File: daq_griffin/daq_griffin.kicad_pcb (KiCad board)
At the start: 4 copper layers, 85 x 120 mm, 191 parts, among them J13 SENSOR, J14 SENSOR, J15 SENSOR, J16 SENSOR, J17 SENSOR, J18 SENSOR, J19 SENSOR, J20 SENSOR, J21 SENSOR, J22 SENSOR, J23 SENSOR, J24 SENSOR, J25 POWER_12V, J26 I2C Header, J27 CAN Header, U13 ADS8866, U14 ADS8866, U15 ADS8866, U16 ADS8866, U17 ADS8866, U18 ADS8866, U19 ADS8866, U20 ADS8866, U21 ADS8866, U22 ADS8866, U23 ADS8866, U24 ADS8866, U25 TPS54302, U26 Teensy4.1, U29 REF6050xDGK, U30 TLV70933, U55 TCAN3414

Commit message: Add files via upload
one 5 V plane contained only 2 connections, so it was replaced with a single wire
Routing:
- net +5V: track 108.8 -> 127.1 mm, vias 4 -> 2
- removed copper zone on In1.Cu, net +5V
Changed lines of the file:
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@@
 	)
 	(via
-		(at 154.4 80.4)
-		(size 0.8)
-		(drill 0.4)
-		(layers "F.Cu" "B.Cu")
-		(net 7)
-	)
-	(via
 		(at 138.888 73.438)
 		(size 0.8)
@@
 	)
 	(via
-		(at 118.4 79.2)
-		(size 0.8)
-		(drill 0.4)
-		(layers "F.Cu" "B.Cu")
-		(net 7)
-	)
-	(via
 		(at 125.1985 73.438)
 		(size 0.8)
@@
 	)
 	(segment
+		(start 138.888 73.438)
+		(end 147.438 73.438)
+		(width 1)
+		(layer "B.Cu")
+		(net 7)
+	)
+	(segment
 		(start 154.42 89.408)
 		(end 154.42 80.42)
@@
 	)
 	(segment
-		(start 154.42 80.42)
-		(end 154.4 80.4)
-		(width 1)
-		(layer "B.Cu")
-		(net 7)
-	)
-	(segment
 		(start 123.971001 83.759)
 		(end 123.971001 81.99)
@@
 	)
 	(segment
-		(start 118.304501 79.104501)
-		(end 118.4 79.2)
-		(width 1)
-		(layer "B.Cu")
-		(net 7)
-	)
-	(segment
 		(start 122.495501 75.438)
 		(end 123.1985 75.438)
@@
 	)
 	(segment
+		(start 147.438 73.438)
+		(end 154.42 80.42)
+		(width 1)
+		(layer "B.Cu")
+		(net 7)
+	)
+	(segment
 		(start 166.584 91.273)
 		(end 166.584 93.853)
@@
 			)
 		)
-	)
-	(zone
-		(net 7)
-		(net_name "+5V")
-		(layer "In1.Cu")
-		(hatch edge 0.508)
-		(connect_pads
-			(clearance 0)
-		)
-		(min_thickness 0.254)
-		(filled_areas_thickness no)
-		(fill yes
-			(thermal_gap 0.508)
-			(thermal_bridge_width 0.508)
-		)
-		(polygon
-			(pts
-				(xy 169.2 81.6) (xy 110.6 81.6) (xy 110.6 77.1) (xy 169.2 77.1)
-			)
-		)

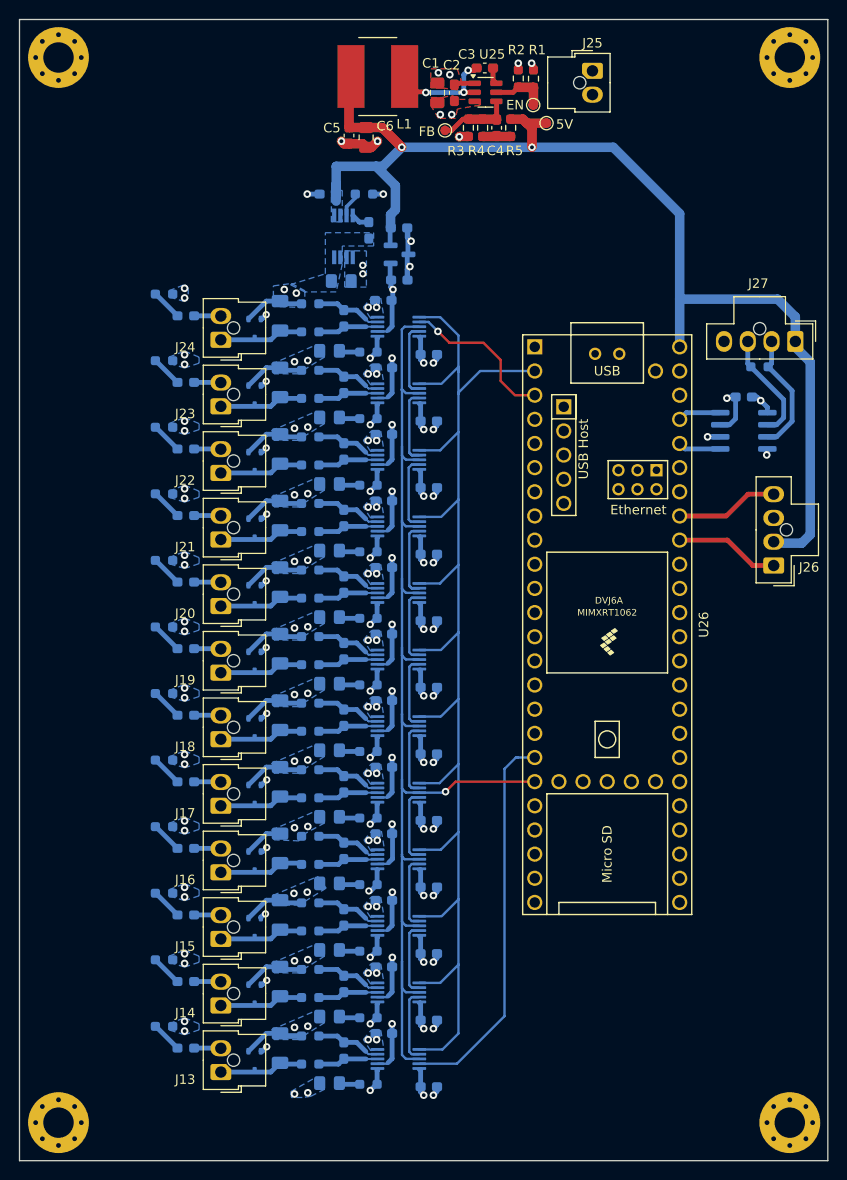
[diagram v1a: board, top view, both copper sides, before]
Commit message: Add thermocouple connectors and minor layout changes.
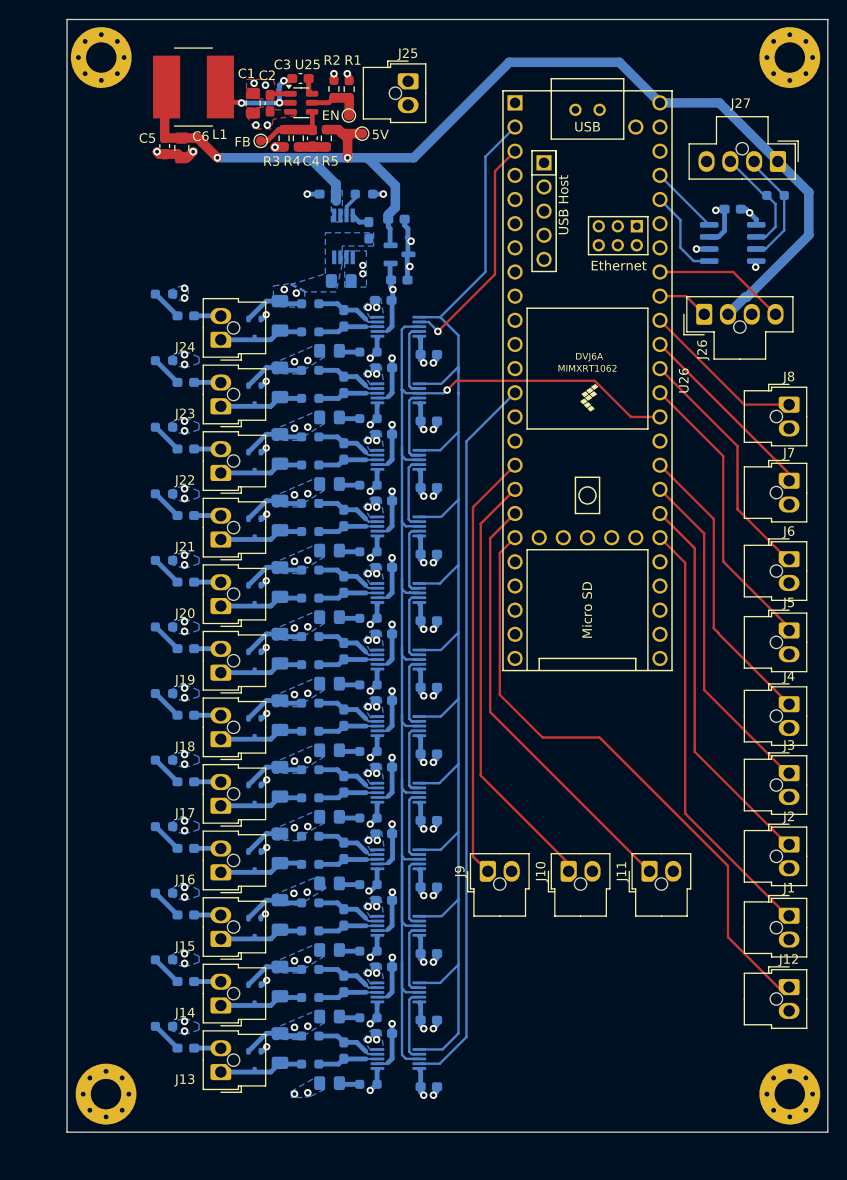
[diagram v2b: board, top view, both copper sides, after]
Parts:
- removed C7: 100nF, Capacitor_SMD:C_0603_1608Metric_Pad1.08x0.95mm_HandSolder
- added C111: 100nF, Capacitor_SMD:C_0603_1608Metric_Pad1.08x0.95mm_HandSolder, B.Cu at (124.6, 81.0)
- added J1: SENSOR, Connector_Molex:Molex_Nano-Fit_105309-xx02_1x02_P2.50mm_Vertical, F.Cu at (165.9, 154.2)
- added J10: SENSOR, Connector_Molex:Molex_Nano-Fit_105309-xx02_1x02_P2.50mm_Vertical, F.Cu at (142.8, 149.6)
- added J11: SENSOR, Connector_Molex:Molex_Nano-Fit_105309-xx02_1x02_P2.50mm_Vertical, F.Cu at (151.2, 149.6)
- added J12: SENSOR, Connector_Molex:Molex_Nano-Fit_105309-xx02_1x02_P2.50mm_Vertical, F.Cu at (165.9, 161.8)
- added J2: SENSOR, Connector_Molex:Molex_Nano-Fit_105309-xx02_1x02_P2.50mm_Vertical, F.Cu at (165.9, 146.8)
- added J3: SENSOR, Connector_Molex:Molex_Nano-Fit_105309-xx02_1x02_P2.50mm_Vertical, F.Cu at (165.9, 139.2)
- added J4: SENSOR, Connector_Molex:Molex_Nano-Fit_105309-xx02_1x02_P2.50mm_Vertical, F.Cu at (165.9, 132.0)
- added J5: SENSOR, Connector_Molex:Molex_Nano-Fit_105309-xx02_1x02_P2.50mm_Vertical, F.Cu at (165.9, 124.2)
- added J6: SENSOR, Connector_Molex:Molex_Nano-Fit_105309-xx02_1x02_P2.50mm_Vertical, F.Cu at (165.9, 116.8)
- added J7: SENSOR, Connector_Molex:Molex_Nano-Fit_105309-xx02_1x02_P2.50mm_Vertical, F.Cu at (165.9, 108.5)
- added J8: SENSOR, Connector_Molex:Molex_Nano-Fit_105309-xx02_1x02_P2.50mm_Vertical, F.Cu at (165.9, 100.5)
- added J9: SENSOR, Connector_Molex:Molex_Nano-Fit_105309-xx02_1x02_P2.50mm_Vertical, F.Cu at (134.2, 149.6)
- moved J26 27.4 mm to (157.0, 91.0), turned to 90 degrees
- moved U26 25.7 mm to (144.7, 98.0)
- moved U55 19.8 mm to (160.0, 83.5)
- moved C113 19.8 mm to (160.0, 79.9)
- moved C3 19.4 mm to (114.5, 66.2)
- moved C4 19.4 mm to (115.8, 72.5)
- moved R1 19.4 mm to (119.7, 67.3)
- moved TP2 19.4 mm to (110.4, 72.8)
- moved C1 19.4 mm to (109.6, 68.8)
- moved C5 19.4 mm to (100.3, 73.3)
- moved C6 19.4 mm to (102.1, 73.5)
- moved J25 19.4 mm to (125.9, 66.5)
- moved L1 19.4 mm to (103.3, 67.1)
- moved R3 19.4 mm to (112.8, 72.5)
- moved R5 19.4 mm to (117.3, 72.5)
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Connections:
- U26 pad 13: unconnected-(U26-11_MOSI_CTX1-Pad13) -> /MOSI2
- U26 pad 16: unconnected-(U26-24_A10_TX6_SCL2-Pad16) -> Net-(J9-Pin_1)
- U26 pad 17: unconnected-(U26-25_A11_RX6_SDA2-Pad17) -> Net-(J10-Pin_1)
- U26 pad 18: /MOSI2 -> Net-(J11-Pin_1)
- U26 pad 19: /SCLK2 -> Net-(J12-Pin_1)
- U26 pad 30: unconnected-(U26-38_CS1_IN1-Pad30) -> Net-(J1-Pin_1)
- U26 pad 31: unconnected-(U26-39_MISO1_OUT1A-Pad31) -> Net-(J2-Pin_1)
- U26 pad 32: unconnected-(U26-40_A16-Pad32) -> Net-(J3-Pin_1)
- U26 pad 33: unconnected-(U26-41_A17-Pad33) -> Net-(J4-Pin_1)
- U26 pad 35: unconnected-(U26-13_SCK_LED-Pad35) -> /SCLK2
- U26 pad 36: unconnected-(U26-14_A0_TX3_SPDIF_OUT-Pad36) -> Net-(J5-Pin_1)
- U26 pad 37: unconnected-(U26-15_A1_RX3_SPDIF_IN-Pad37) -> Net-(J6-Pin_1)
- U26 pad 38: unconnected-(U26-16_A2_RX4_SCL1-Pad38) -> Net-(J7-Pin_1)
- U26 pad 39: unconnected-(U26-17_A3_TX4_SDA1-Pad39) -> Net-(J8-Pin_1)
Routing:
- net Net-(J12-Pin_1): track 0.00 -> 64.7 mm
- net Net-(J11-Pin_1): track 0.00 -> 45.6 mm
- net Net-(J1-Pin_1): track 0.00 -> 45.5 mm
- net Net-(J10-Pin_1): track 0.00 -> 45.5 mm
- net Net-(J9-Pin_1): track 0.00 -> 45.2 mm
- net Net-(J2-Pin_1): track 0.00 -> 40.5 mm
- net Net-(J3-Pin_1): track 0.00 -> 35.6 mm
- net /MOSI2: track 40.7 -> 76.0 mm
- net Net-(J4-Pin_1): track 0.00 -> 30.8 mm
- net Net-(J5-Pin_1): track 0.00 -> 30.6 mm
- net Net-(J6-Pin_1): track 0.00 -> 25.8 mm
- net Net-(J7-Pin_1): track 0.00 -> 20.0 mm
- net Net-(J8-Pin_1): track 0.00 -> 17.3 mm
- net /SCLK2: track 126.9 -> 142.7 mm
- net /ADC_Chain2/CS: track 141.2 -> 155.5 mm
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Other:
- board size 85 x 120 mm -> 80 x 117 mm
